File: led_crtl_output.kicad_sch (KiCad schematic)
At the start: 3 parts, among them U26 74LVC1G17GW,125

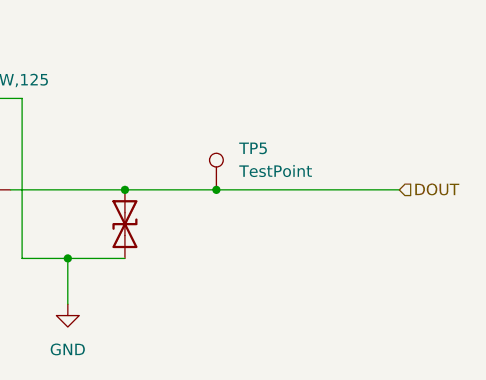
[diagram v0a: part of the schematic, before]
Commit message: Place opto couplers and some connectors.
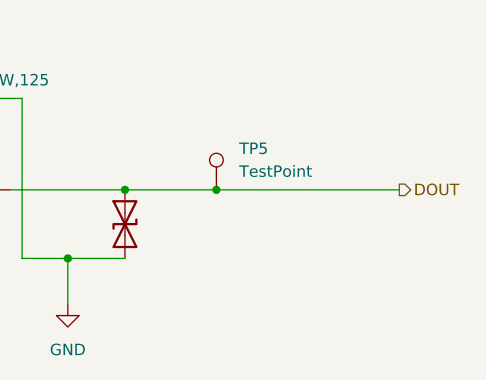
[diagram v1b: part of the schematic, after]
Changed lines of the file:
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@@
 	)
 	(hierarchical_label "DOUT"
-		(shape input)
+		(shape output)
 		(at 121.92 62.23 0)
 		(effects

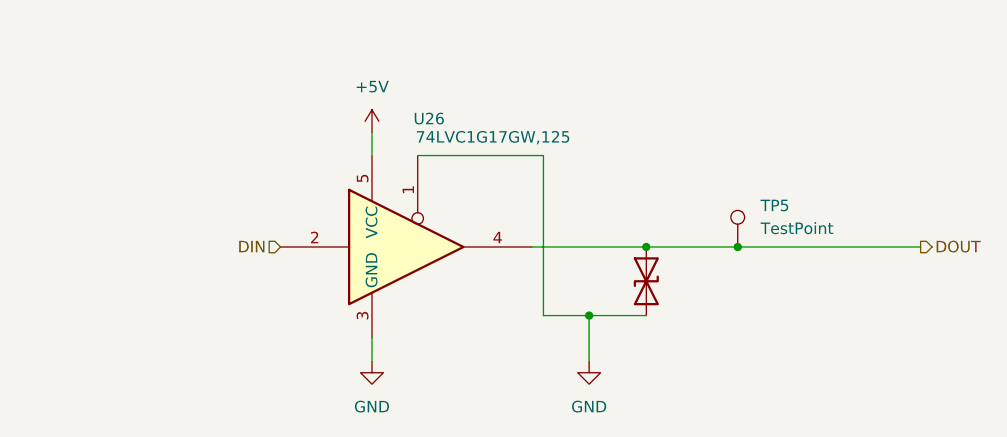
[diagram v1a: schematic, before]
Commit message: changed driver IC for LED signal to 74HCT1G125GW
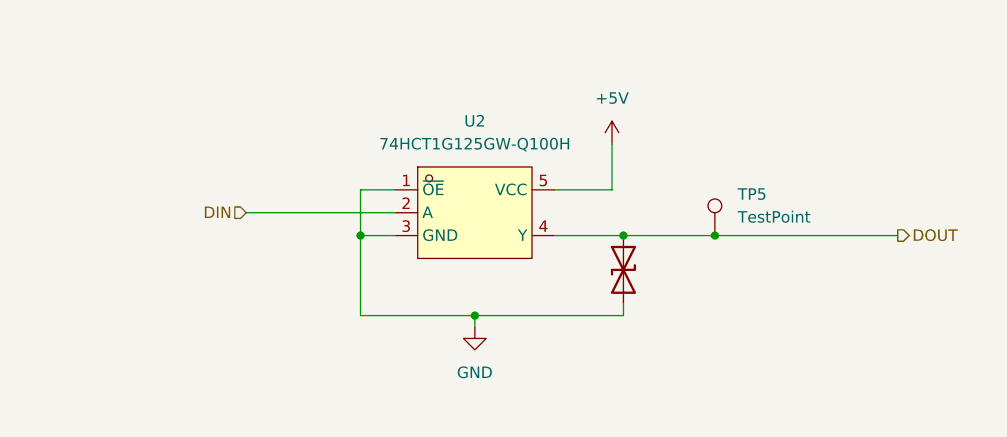
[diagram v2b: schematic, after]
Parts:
- removed U26: 74LVC1G17GW,125, Package_TO_SOT_SMD:SOT-353_SC-70-5, symbol 74xGxx:74LVC1G125
- added U2: 74HCT1G125GW-Q100H, lcsc:TSSOP-5_L2.1-W1.3-P0.65-LS2.2-BL, symbol lcsc:74HCT1G125GW-Q100H
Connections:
- net +5V: now also U2.5 (VCC)
- net DIN: now also U2.2 (A)
- net DOUT: now also U2.4 (Y)
- net GND: now also U2.1 (~{OE}), U2.3 (GND)
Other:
- moved on the sheet: TP5

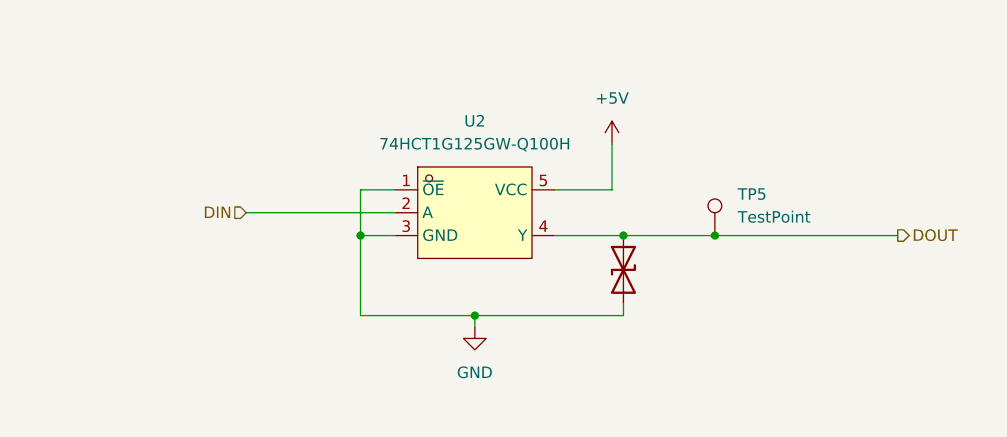
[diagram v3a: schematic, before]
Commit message: Fixed fabrication files, so PCBA will work with the correct rotation of the components.
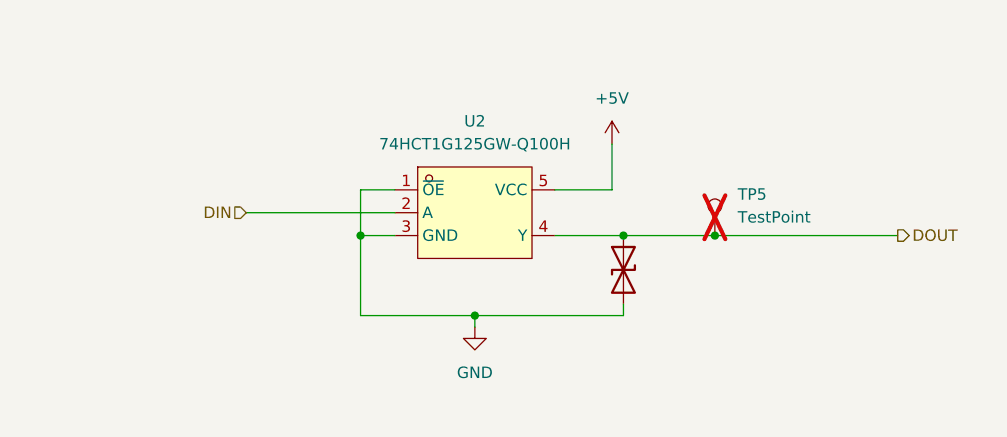
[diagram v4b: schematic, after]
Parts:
- TP5: now not fitted; now left out of the parts list
- U2: LCSC Part C547449 -> C547448; Rotation Offset (none) -> 90
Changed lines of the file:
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@@
 			)
 		)
-		(property "Datasheet" "https://lcsc.com/product-detail/presales_Nexperia-74HCT1G125GW-Q100H_C547449.html"
+		(property "Datasheet" "https://jlcpcb.com/partdetail/Nexperia-74HCT1G125GW125/C547448"
 			(at 71.12 71.12 0)
 			(effects
@@
 			)
 		)
-		(property "LCSC Part" "C547449"
+		(property "LCSC Part" "C547448"
 			(at 71.12 73.66 0)
+			(effects
+				(font
+					(size 1.27 1.27)
+				)
+				(hide yes)
+			)
+		)
+		(property "gnd" ""
+			(at 71.12 58.42 0)
+			(effects
+				(font
+					(size 1.27 1.27)
+				)
+				(hide yes)
+			)
+		)
+		(property "input1" ""
+			(at 71.12 58.42 0)
+			(effects
+				(font
+					(size 1.27 1.27)
+				)
+				(hide yes)
+			)
+		)
+		(property "input2" ""
+			(at 71.12 58.42 0)
+			(effects
+				(font
+					(size 1.27 1.27)
+				)
+				(hide yes)
+			)
+		)
+		(property "input3" ""
+			(at 71.12 58.42 0)
+			(effects
+				(font
+					(size 1.27 1.27)
+				)
+				(hide yes)
+			)
+		)
+		(property "Rotation Offset" "90"
+			(at 71.12 58.42 0)
 			(effects
 				(font
@@
 			)
 		)
+		(property "gnd" ""
+			(at 88.9 64.77 0)
+			(effects
+				(font
+					(size 1.27 1.27)
+				)
+				(hide yes)
+			)
+		)
+		(property "input1" ""
+			(at 88.9 64.77 0)
+			(effects
+				(font
+					(size 1.27 1.27)
+				)
+				(hide yes)
+			)
+		)
+		(property "input2" ""
+			(at 88.9 64.77 0)
+			(effects
+				(font
+					(size 1.27 1.27)
+				)
+				(hide yes)
+			)
+		)
+		(property "input3" ""
+			(at 88.9 64.77 0)
+			(effects
+				(font
+					(size 1.27 1.27)
+				)
+				(hide yes)
+			)
+		)
 		(pin "2"
 		)
@@
 		(unit 1)
 		(exclude_from_sim no)
-		(in_bom yes)
+		(in_bom no)
 		(on_board yes)
-		(dnp no)
+		(dnp yes)
 		(fields_autoplaced yes)
 		(property "Reference" "TP5"
@@
 			(at 99.06 60.96 0)
 			(effects
+				(font
+					(size 1.27 1.27)
+				)
+				(hide yes)
+			)
+		)
+		(property "gnd" ""
+			(at 99.06 60.96 0)
+			(effects
+				(font
+					(size 1.27 1.27)
+				)
+				(hide yes)
+			)
+		)
+		(property "input1" ""
+			(at 99.06 60.96 0)
+			(effects
+				(font
+					(size 1.27 1.27)
+				)
+				(hide yes)
+			)
+		)
+		(property "input2" ""
+			(at 99.06 60.96 0)
+			(effects
+				(font
+					(size 1.27 1.27)
+				)
+				(hide yes)
+			)
+		)
+		(property "input3" ""
+			(at 99.06 60.96 0)
+			(effects

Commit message: Fixed issue with too little of a component for second prod run.
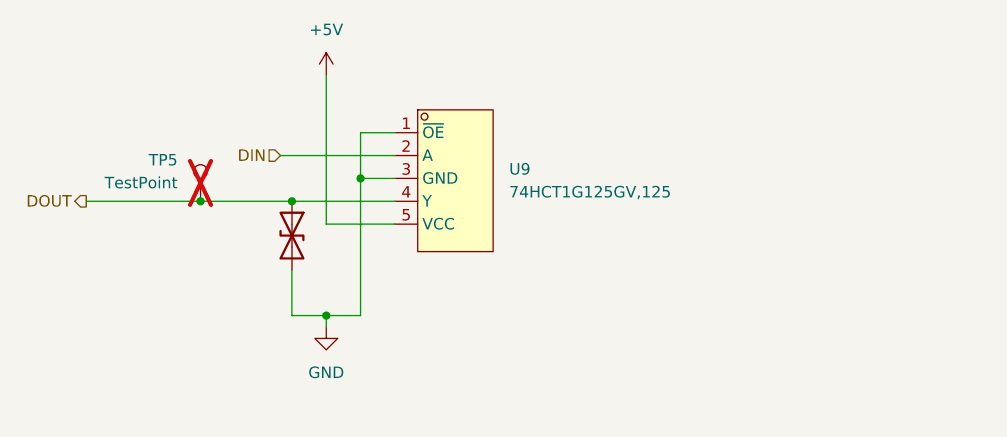
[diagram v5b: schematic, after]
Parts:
- removed U2: 74HCT1G125GW-Q100H, lcsc:TSSOP-5_L2.1-W1.3-P0.65-LS2.2-BL, symbol lcsc:74HCT1G125GW-Q100H
- added U9: 74HCT1G125GV,125, lcsc:SOT-753_L3.1-W1.7-P0.95-LS3.0-BL, symbol lcsc:74HCT1G125GV,125
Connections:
- net +5V: now also U9.5 (VCC)
- net DIN: now also U9.2 (A)
- net DOUT: now also U9.4 (Y)
- net GND: now also U9.1 (~{OE}), U9.3 (GND)
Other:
- moved on the sheet: TP5
